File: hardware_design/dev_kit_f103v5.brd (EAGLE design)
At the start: 56.8 x 69.3 mm, 57 parts, among them J2 CON-SD-CARD_MICROSD-2908-05, U2 FT232RLSSOP, Y1 32.768kHz

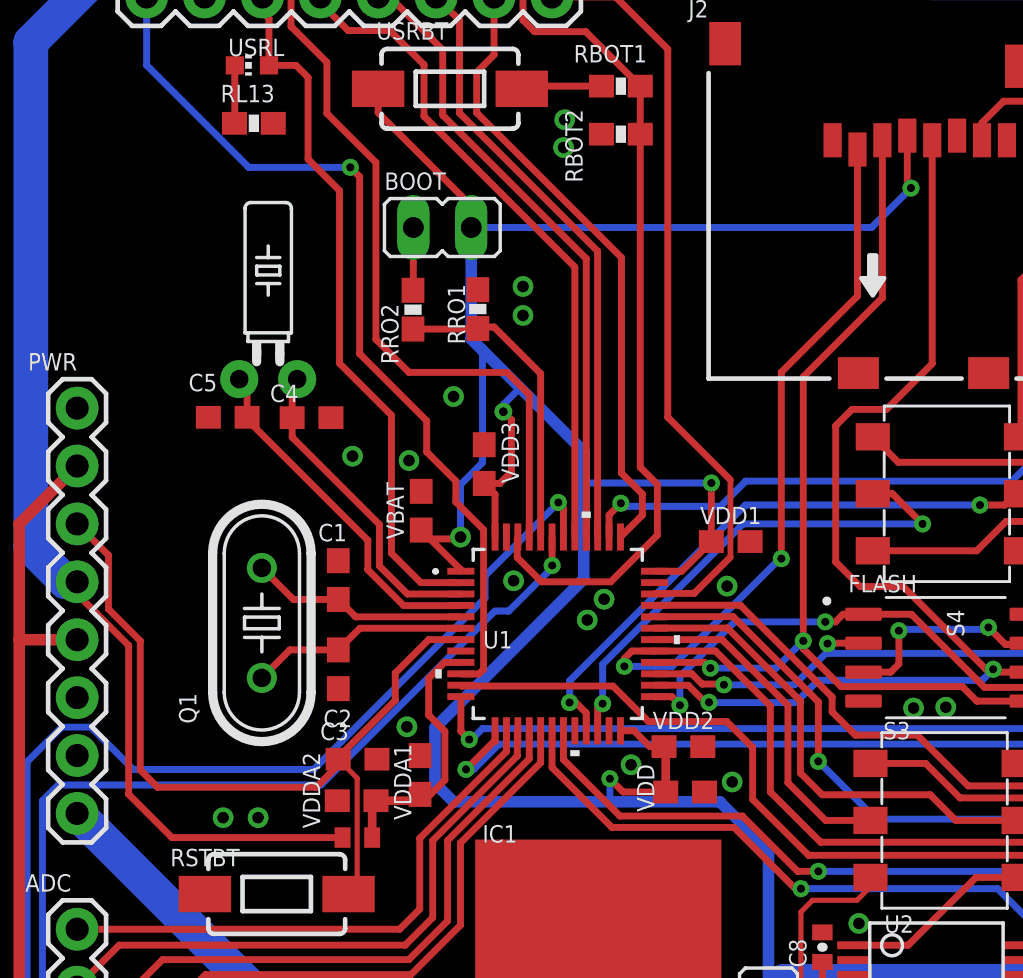
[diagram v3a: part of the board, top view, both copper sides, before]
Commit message: Polygon witdh was increased IMPORTANT**
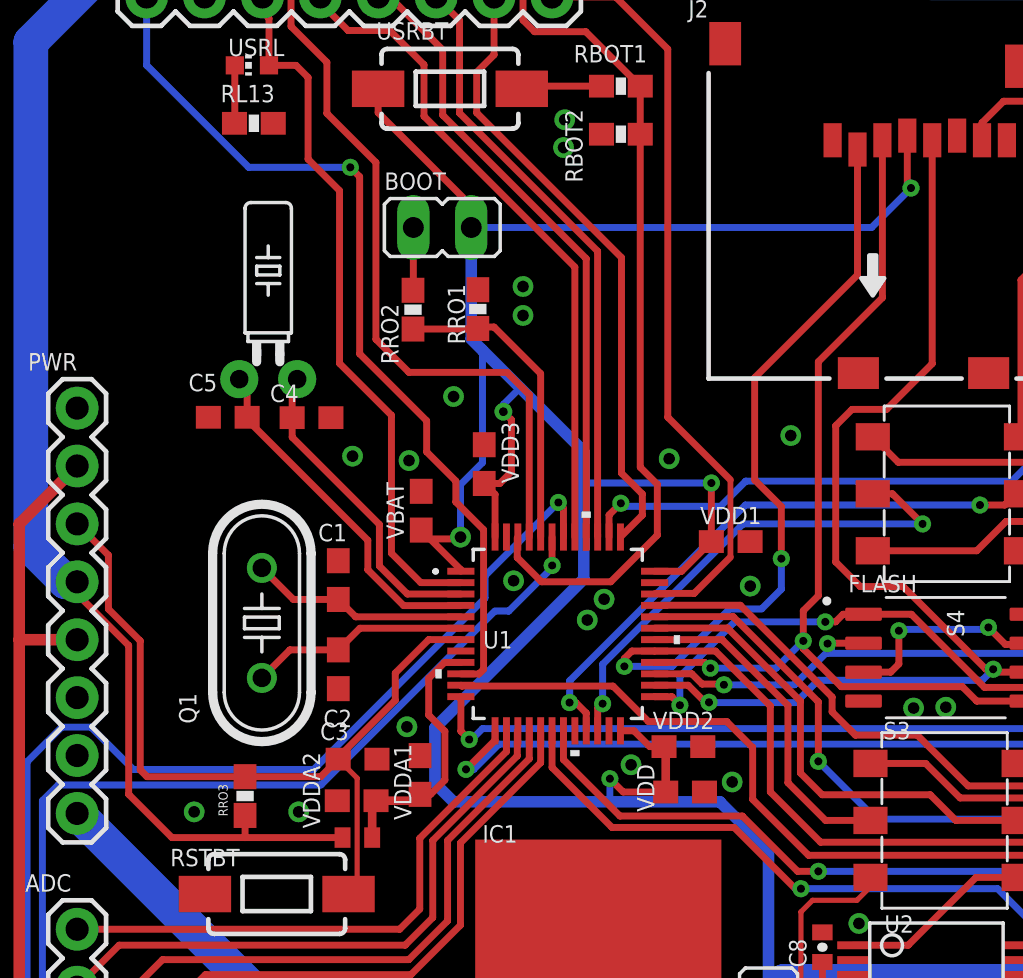
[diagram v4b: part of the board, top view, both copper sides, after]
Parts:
- added RRO3: 10k, SparkFun-Resistors:0603-RES
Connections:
- net 3.3V: now also RRO3.1
- net NRST: now also RRO3.2
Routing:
- net PA8: track 60.2 -> 61.9 mm
- net 3.3V: track 332.5 -> 333.4 mm
- net NRST: track 36.3 -> 35.8 mm
- net GND: vias 23 -> 25
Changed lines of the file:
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@@
 <attribute name="VALUE" x="64.262" y="28.19" size="0.6096" layer="27" font="vector" ratio="20" rot="R90"/>
+</element>
+<element name="RRO3" library="SparkFun-Resistors" package="0603-RES" value="10k" x="21.336" y="26.162" smashed="yes" rot="R90">
+<attribute name="NAME" x="20.574" y="25.273" size="0.4064" layer="25" font="vector" rot="R90"/>
+<attribute name="PROD_ID" value="RES-08296" x="21.336" y="26.162" size="1.778" layer="27" rot="R90" display="off"/>
+<attribute name="VALUE" x="22.479" y="25.146" size="0.4064" layer="27" font="vector" rot="R90"/>
 </element>
 </elements>
@@
 <contactref element="J2" pad="6"/>
 <contactref element="J1" pad="7"/>
-<polygon width="0.1524" layer="1">
+<polygon width="0.3048" layer="1">
 <vertex x="8.89" y="70.104"/>
 <vertex x="67.9704" y="70.104"/>
@@
 <vertex x="8.89" y="-2.83971875"/>
 </polygon>
-<polygon width="0.1524" layer="16">
+<polygon width="0.3048" layer="16">
 <vertex x="7.62" y="71.12"/>
 <vertex x="7.62" y="-4.030978125"/>
@@
 <via x="30.48" y="43.688" extent="1-16" drill="0.508"/>
 <via x="37.084" y="34.798" extent="1-16" drill="0.508"/>
-<via x="21.9075" y="25.21458125" extent="1-16" drill="0.508"/>
-<via x="42.4789625" y="35.372040625" extent="1-16" drill="0.508"/>
+<via x="23.6855" y="25.46858125" extent="1-16" drill="0.508"/>
+<via x="43.4949625" y="35.372040625" extent="1-16" drill="0.508"/>
 <via x="57.4802" y="3.429" extent="1-16" drill="0.508"/>
 <wire x1="55.4736" y1="4.0894" x2="56.134" y2="3.429" width="0.3048" layer="1"/>
@@
 <wire x1="56.7736" y1="5.3894" x2="55.4736" y2="4.0894" width="0.3048" layer="1"/>
 <via x="28.4353" y="29.199840625" extent="1-16" drill="0.508"/>
-<via x="20.373340625" y="25.214578125" extent="1-16" drill="0.508"/>
+<via x="19.103340625" y="25.468578125" extent="1-16" drill="0.508"/>
 <via x="50.038" y="14.351" extent="1-16" drill="0.508"/>
 <via x="52.072540625" y="30.058359375" extent="1-16" drill="0.508"/>
@@
 <via x="42.70248125" y="26.779221875" extent="1-16" drill="0.508"/>
 <via x="28.526740625" y="40.878759375" extent="1-16" drill="0.508"/>
+<via x="39.9389625" y="40.960040625" extent="1-16" drill="0.508"/>
+<via x="45.2729625" y="41.976040625" extent="1-16" drill="0.508"/>
 </signal>
 <signal name="3.3V">
@@
 <wire x1="16.2306" y1="32.766" x2="16.2306" y2="26.2382" width="0.3048" layer="1"/>
 <wire x1="16.2306" y1="26.2382" x2="18.12798125" y2="24.34081875" width="0.3048" layer="1"/>
-<wire x1="18.12798125" y1="24.34081875" x2="25.61105625" y2="24.34081875" width="0.3048" layer="1"/>
+<wire x1="18.12798125" y1="24.34081875" x2="21.336" y2="24.34081875" width="0.3048" layer="1"/>
+<wire x1="21.336" y1="24.34081875" x2="25.61105625" y2="24.34081875" width="0.3048" layer="1"/>
 <wire x1="13.97" y1="35.0266" x2="16.2306" y2="32.766" width="0.3048" layer="1"/>
 <wire x1="29.6672" y1="26.7208" x2="29.6672" y2="29.1592" width="0.508" layer="16"/>
@@
 <wire x1="33.02" y1="40.386" x2="32.507815625" y2="39.873815625" width="0.3048" layer="1"/>
 <wire x1="32.507815625" y1="39.873815625" x2="31.8262" y2="39.873815625" width="0.3048" layer="1"/>
+<contactref element="RRO3" pad="1"/>
+<wire x1="21.336" y1="25.312" x2="21.336" y2="24.34081875" width="0.3048" layer="1"/>
 </signal>
 <signal name="VIN">
@@
 <wire x1="15.3416" y1="36.7284" x2="13.97" y2="38.1" width="0.3048" layer="1"/>
 <wire x1="16.7386" y1="32.9692" x2="16.7386" y2="27.305" width="0.3048" layer="1"/>
-<wire x1="25.421225" y1="27.515825" x2="25.421225" y2="27.779978125" width="0.2286" layer="1"/>
-<wire x1="25.421225" y1="27.515825" x2="24.453478125" y2="26.548078125" width="0.3048" layer="1"/>
-<wire x1="16.7386" y1="27.305" x2="17.495521875" y2="26.548078125" width="0.3048" layer="1"/>
-<wire x1="17.495521875" y1="26.548078125" x2="24.453478125" y2="26.548078125" width="0.3048" layer="1"/>
+<contactref element="RRO3" pad="2"/>
+<wire x1="25.421225" y1="27.779978125" x2="24.653246875" y2="27.012" width="0.3048" layer="1"/>
+<wire x1="24.653246875" y1="27.012" x2="21.336" y2="27.012" width="0.3048" layer="1"/>
+<wire x1="21.336" y1="27.012" x2="17.0316" y2="27.012" width="0.3048" layer="1"/>
+<wire x1="17.0316" y1="27.012" x2="16.7386" y2="27.305" width="0.3048" layer="1"/>
 </signal>
 <signal name="BOOT0">
@@
 <wire x1="62.23" y1="37.08" x2="63.5" y2="35.81" width="0.3048" layer="1"/>
 <wire x1="63.5" y1="35.81" x2="63.5" y2="31.2206" width="0.3048" layer="1"/>
-<wire x1="49.2927" y1="54.9287" x2="49.2927" y2="48.0227" width="0.3048" layer="1"/>
-<wire x1="49.2927" y1="48.0227" x2="45.8216" y2="44.5516" width="0.3048" layer="1"/>
-<wire x1="45.8216" y1="44.5516" x2="45.8216" y2="32.966659375" width="0.3048" layer="1"/>
+<wire x1="49.2927" y1="48.0227" x2="49.2927" y2="54.9287" width="0.3048" layer="1"/>
+<wire x1="45.8216" y1="32.966659375" x2="45.8216" y2="34.29" width="0.3048" layer="1"/>
 <wire x1="55.675" y1="30.3276" x2="59.0296" y2="30.3276" width="0.3048" layer="1"/>
 <wire x1="59.0296" y1="30.3276" x2="59.436" y2="30.734" width="0.3048" layer="1"/>
@@
 <wire x1="53.43218125" y1="30.3276" x2="52.799721875" y2="30.960059375" width="0.3048" layer="1"/>
 <wire x1="52.799721875" y1="30.960059375" x2="47.485303125" y2="30.960059375" width="0.3048" layer="1"/>
+<wire x1="45.8216" y1="34.29" x2="46.482" y2="34.9504" width="0.3048" layer="1"/>
+<wire x1="46.482" y1="34.9504" x2="46.482" y2="45.212" width="0.3048" layer="1"/>
+<wire x1="46.482" y1="45.212" x2="49.2927" y2="48.0227" width="0.3048" layer="1"/>
 </signal>
 <signal name="MISO2">
@@
 <wire x1="44.376340625" y1="30.11678125" x2="41.969121875" y2="32.524" width="0.3048" layer="1"/>
 <wire x1="41.969121875" y1="32.524" x2="39.302" y2="32.524" width="0.3048" layer="1"/>
-<wire x1="48.2005" y1="54.5223" x2="48.2005" y2="48.096359375" width="0.3048" layer="1"/>
-<wire x1="44.8592" y1="44.755059375" x2="44.8592" y2="36.576" width="0.3048" layer="1"/>
+<wire x1="48.2005" y1="49.022" x2="48.2005" y2="54.5223" width="0.3048" layer="1"/>
 <via x="44.8592" y="36.576" extent="1-16" drill="0.35"/>
-<wire x1="44.8592" y1="36.576" x2="44.798240625" y2="36.576" width="0.3048" layer="16"/>
-<wire x1="44.798240625" y1="36.576" x2="40.073840625" y2="31.8516" width="0.3048" layer="16"/>
+<wire x1="44.8592" y1="36.576" x2="44.8592" y2="38.862" width="0.3048" layer="1"/>
+<wire x1="40.073840625" y1="31.8516" x2="42.592121875" y2="34.36988125" width="0.3048" layer="16"/>
 <wire x1="40.073840625" y1="31.8516" x2="37.973" y2="31.8516" width="0.3048" layer="16"/>
 <via x="37.973" y="31.8516" extent="1-16" drill="0.35"/>
@@
 <wire x1="37.973" y1="31.8516" x2="37.973" y2="32.191959375" width="0.3048" layer="1"/>
 <wire x1="38.305040625" y1="32.524" x2="39.302" y2="32.524" width="0.3048" layer="1"/>
-<wire x1="48.2005" y1="48.096359375" x2="44.8592" y2="44.755059375" width="0.3048" layer="1"/>
 <wire x1="62.23" y1="20.32" x2="60.656621875" y2="20.32" width="0.3048" layer="1"/>
 <wire x1="60.656621875" y1="20.32" x2="56.839003125" y2="24.13761875" width="0.3048" layer="1"/>
 <wire x1="44.376340625" y1="26.34223125" x2="46.580953125" y2="24.13761875" width="0.3048" layer="1"/>
 <wire x1="46.580953125" y1="24.13761875" x2="56.839003125" y2="24.13761875" width="0.3048" layer="1"/>
+<wire x1="42.592121875" y1="34.36988125" x2="43.99394375" y2="34.36988125" width="0.3048" layer="16"/>
+<wire x1="44.8592" y1="35.2351375" x2="44.8592" y2="36.576" width="0.3048" layer="16"/>
+<wire x1="43.99394375" y1="34.36988125" x2="44.8592" y2="35.2351375" width="0.3048" layer="16"/>
+<wire x1="44.8592" y1="38.862" x2="43.688" y2="40.0332" width="0.3048" layer="1"/>
+<wire x1="43.688" y1="44.5095" x2="48.2005" y2="49.022" width="0.3048" layer="1"/>
+<wire x1="43.688" y1="40.0332" x2="43.688" y2="44.5095" width="0.3048" layer="1"/>
 </signal>
 <signal name="PA11">
